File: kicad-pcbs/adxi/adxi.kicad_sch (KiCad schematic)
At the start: 84 parts, among them J1 FROM-PC-SPK, J10 BANDMODULE3-ANT, J11 BANDMODULE4-ANT, J12 BANDMODULE3-PA, J13 BANDMODULE4-PA, J14 BANDMODULE5-ANT, J15 BANDMODULE6-ANT, J16 BANDMODULE5-PA, J17 BANDMODULE6-PA, J18 MMCX, J19 IPEX-1, J2 TO-PC-MIC, J20 LCD-2004, J3 BNC, J4 SMA, J5 12V SUPPLY, J6 BANDMODULE1-ANT, J7 BANDMODULE1-PA, J8 BANDMODULE2-ANT, J9 BANDMODULE2-PA, Q1 MMBF170, Q2 HY1904C2, U1 CD2003, U2 L7812, U3 74ACT244, U4 Si5351A-B-GT

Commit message: RF choke for 70cm
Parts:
- added L142, L145, L146, L148, L149, L151, L152, L154, L155: 18nH, Inductor_SMD:L_1210_3225Metric, symbol Device:L
- added L143, L144, L147, L150, L153: 33nH, Inductor_SMD:L_1210_3225Metric, symbol Device:L
- L141: value 220uH -> 18nH; footprint (none) -> Inductor_SMD:L_1210_3225Metric; LCSC Part # (none) -> C318035; MPN (none) -> FHW1210HC018JGT; Manufacturer (none) -> Fenghua
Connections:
- net at L141.1: now also L142.1, L143.2
- net at L141.2: now also L142.2, L144.1
- new net: L144.2, L145.1, L146.1
- new net: L145.2, L146.2, L147.1
- new net: L147.2, L148.1, L149.1
- new net: L148.2, L149.2, L150.1
- new net: L150.2, L151.1, L152.1
- new net: L151.2, L152.2, L153.1
- new net: L153.2, L154.1, L155.1
- new net: L154.2, L155.2
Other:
- note added: "0.8Ω 210nH 1A SRF=1800MHz"
- note removed: "SHARED ACROSS ALL FREQUENCY BANDS. SRF > 140MHz"

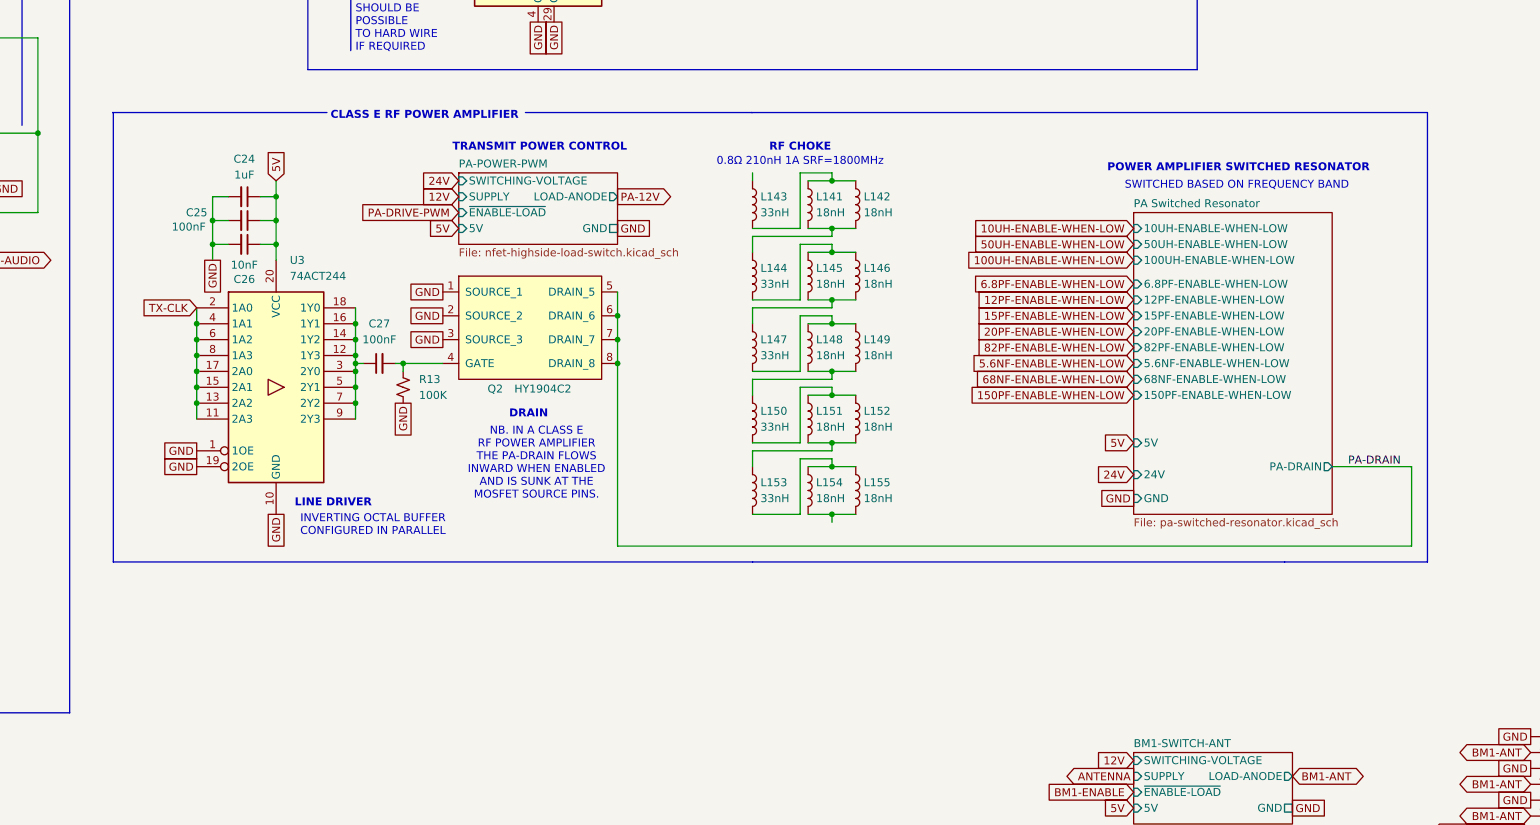
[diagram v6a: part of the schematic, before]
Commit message: Closer to functional PA
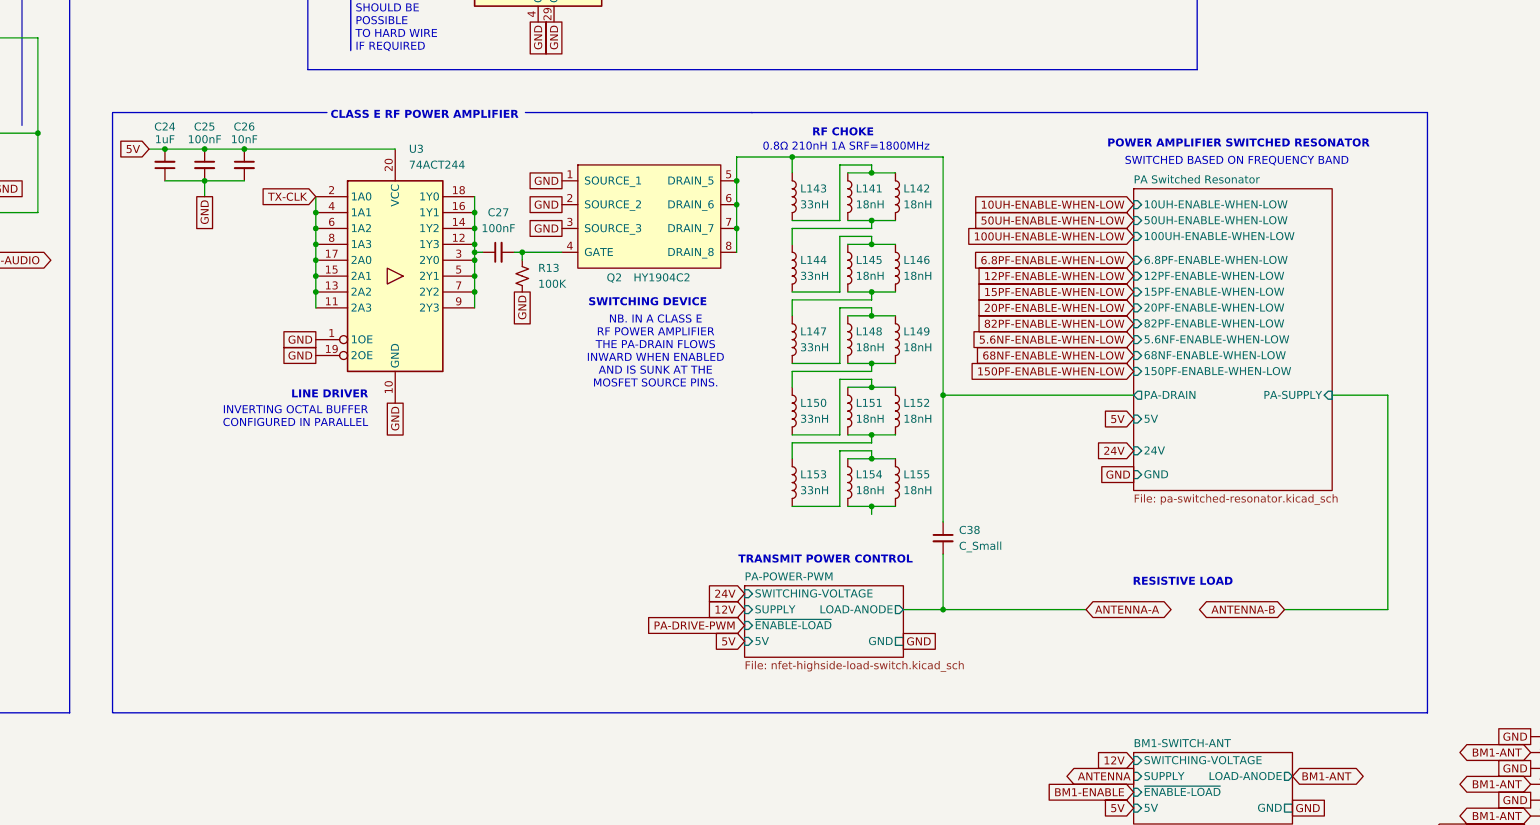
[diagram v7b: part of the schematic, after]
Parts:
- added C38: C_Small, symbol Device:C_Small
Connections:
- net 5V: now also C24.2; no longer C24.1
- net GND: now also C24.1; no longer C24.2
- net PA-DRAIN: no longer Q2.5 (DRAIN_5), Q2.6 (DRAIN_6), Q2.7 (DRAIN_7), Q2.8 (DRAIN_8)
- net PA Switched Resonator/PA-DRAIN: now reaches L143.1
- net PA Switched Resonator/PA-DRAIN: now also Q2.5 (DRAIN_5), Q2.6 (DRAIN_6), Q2.7 (DRAIN_7), Q2.8 (DRAIN_8), C38.1
- new net ANTENNA-A: C38.2
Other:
- sheet PA Switched Resonator ports: added PA-SUPPLY; removed none
- note added: "RESISTIVE LOAD"
- note added: "SWITCHING DEVICE"
- note removed: "DRAIN"
- moved on the sheet: C24, C25, C26, C27, L141, L142, L143, L144, L145, L146, L147, L148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

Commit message: Further PA choke work
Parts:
- added C39: 1pF, Capacitor_SMD:C_0402_1005Metric, symbol Device:C_Small
- added C40: 10pF, Capacitor_SMD:C_0603_1608Metric, symbol Device:C_Small
- added C41: 100pF, Capacitor_SMD:C_0603_1608Metric, symbol Device:C_Small
- added C42: 1nF, Capacitor_SMD:C_0805_2012Metric, symbol Device:C_Small
- added C43: 22nF, Capacitor_SMD:C_1206_3216Metric, symbol Device:C_Small
- added D34: BZT52C5V6, Diode_SMD:D_SOD-123, symbol Device:D_Zener
- added FB2: 100mΩ/3A, Capacitor_SMD:C_1206_3216Metric, symbol Device:FerriteBead_Small
- added L156, L157, L158, L159: 100uH, Inductor_SMD:L_Cenker_CKCS8040, symbol Device:L
- added L160: L, symbol Device:L
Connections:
- net GND: now also C39.2, C40.2, C41.2, C42.2, C43.2, D34.1 (K)
- net PA Switched Resonator/PA-DRAIN: now also FB2.2; no longer L143.1
- net at L154.2, L155.2: now also C39.1, C40.1, C41.1, C42.1, C43.1, D34.2 (A), L159.2
- new net: FB2.1, L143.1, L156.1, L160.1
- new net: L157.2, L158.1
- new net: L158.2, L159.1
- new net: L156.2, L157.1
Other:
- note added: "1.16Ω 400uH >1A SRF=4000MHz"
- note added: "160-2200M / 135kHz-2MHz"
- note added: "2-60M / 5-144MHz"
- note added: "70CM / 450MHz"
- note added: "For 2200m through 160m bands (135 kHz - 2 MHz): Inductance: 100-470 μH (series combination may be necessary) Current rating: 100-500 mA (application dependent) Self-resonant frequency (SRF): Above 2 MHz Package size: 1008 (2520 metric) or larger DCR: As low as possible, typically <1 Ω Recommendations: Use multiple high-value SMD inductors in series Consider ferrite core SMD inductors for higher i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"
- note added: "For 60m through 2m bands (5 MHz - 144 MHz): Inductance: 1-10 μH Current rating: 100-500 mA (application dependent) Self-resonant frequency (SRF): Above 150 MHz Q factor: >50 at operating frequencies Package size: 0805 (2012 metric) or 0603 (1608 metric) DCR: <0.5 Ω Recommendations: Use multi-layer or wire-wound SMD inductors for better Q factor Consider series combination of smaller value inducto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"
- note added: "PROTECTION"
- note added: "RF CHOKE AC GROUND DECOUPLING"
- note added: "SMALLER VALUE CAPACITORS ARE TO BE POSITIONED CLOSER TO RF CHOKE"
- moved on the sheet: C24, C25, C26, C27, C38, L141, L142, L143, L144, L145, L146, L147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
